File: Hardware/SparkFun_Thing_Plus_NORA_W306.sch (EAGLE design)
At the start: 81 parts, among them J1 THING_PLUS_LOGICAL, J2 LiPo, J3 QWIIC_RA, J4 SDFRICTION, J5 USB-C, J6 SWD (DNP), Q1 20V/4.2A/52mΩ/1.4W, Q2 MBT3904DW1T1, Q3 20V/4.2A/52mΩ/1.4W, Q4 20V/4.2A/52mΩ/1.4W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

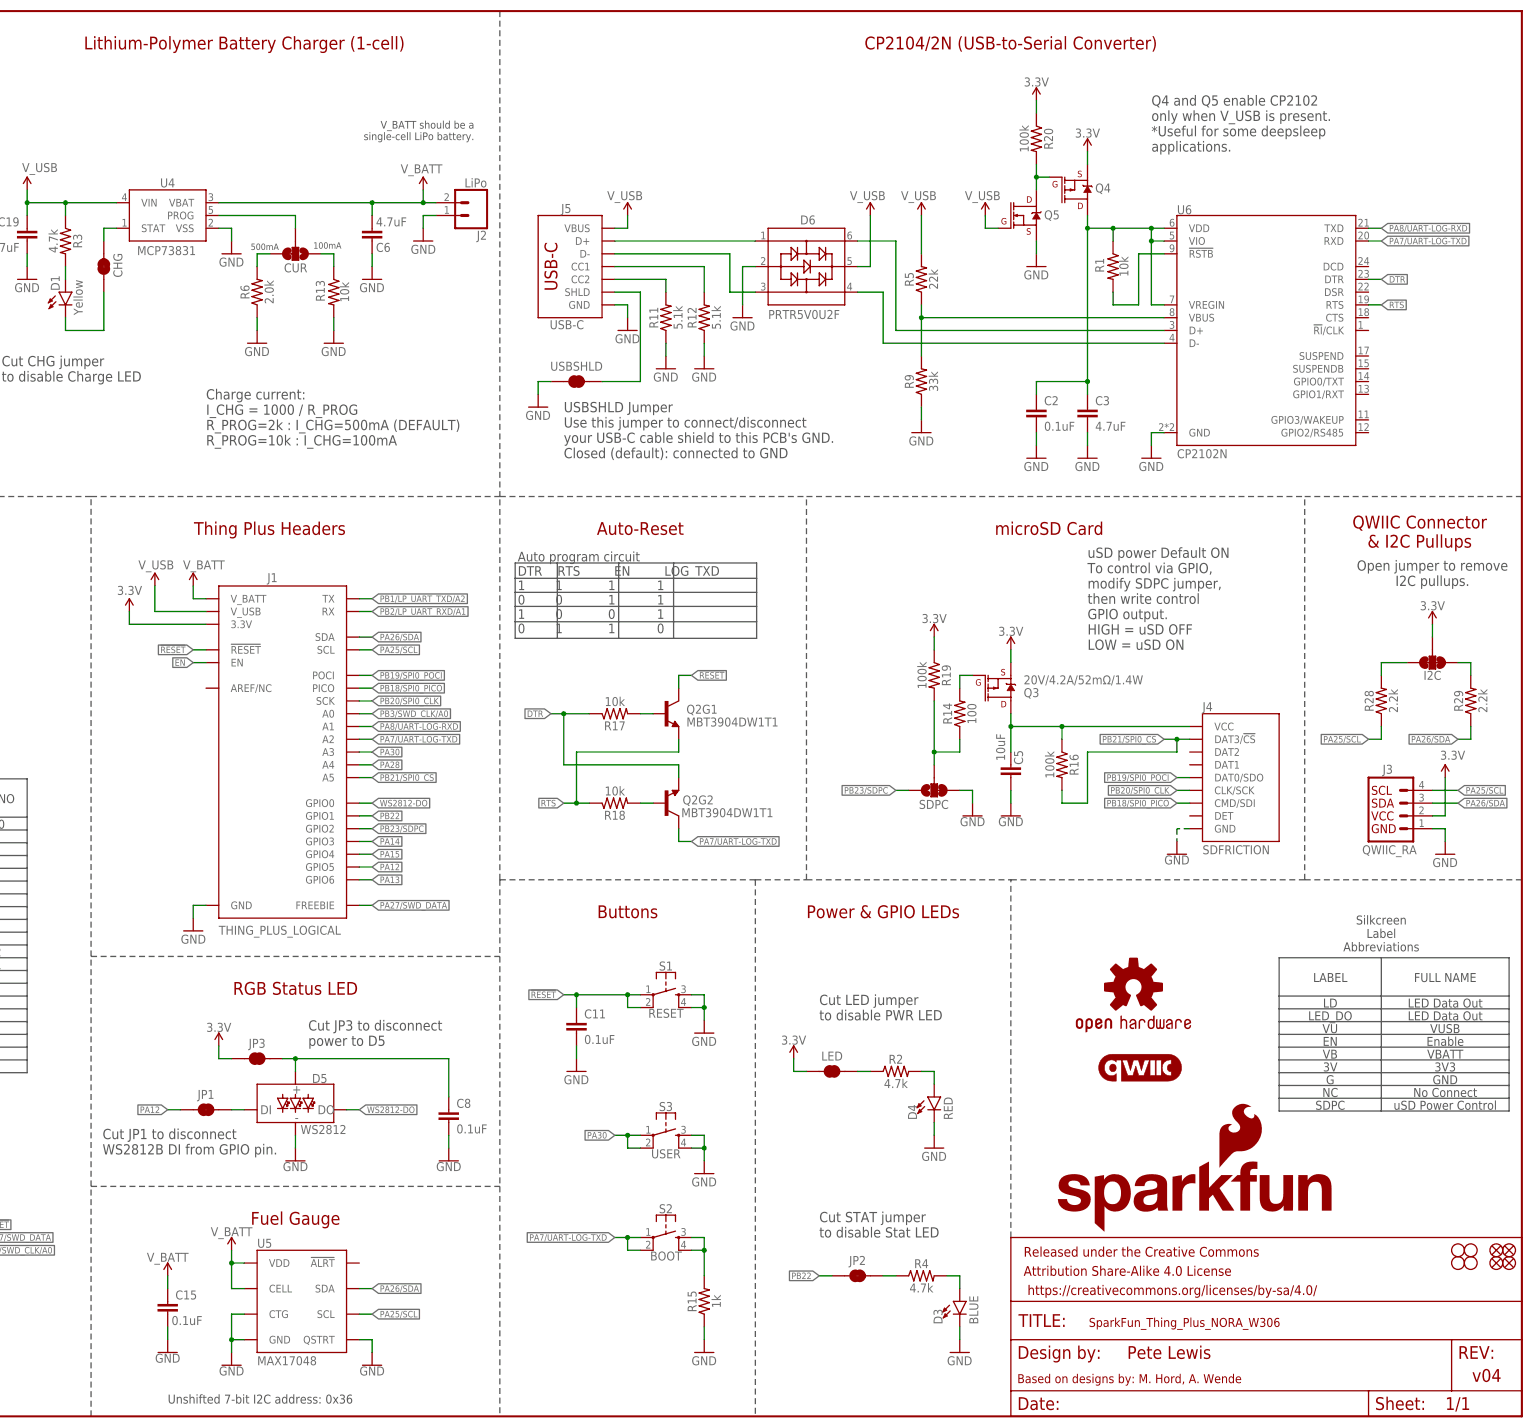
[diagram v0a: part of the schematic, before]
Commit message: final review before ordering proto changes
-added 100 ohm slow down resistor to CP2102 mosfet control gate pin
-added 1K pull down off of SCPC jumper to protect gpio in case user accidentally closes all 3 pads on jumper.
-changed VBATT trace on inner layer so it crosses SDA/SCL at 90
-added gnd via above user botton
-added full size SFE logo to bottom silk
-center product name silk
-redrew bRestrict as rectangles in module FP
-made all sch labels vector
-changed "No connect" to "Not connected" in abbreviation table
-Add note - if user cuts JP3, they should cut JP1 too to prevent back powering
-Add warning - if SDPC is enabled, user needs to not drive pins high until uSD is powered
-changed CUR jumper labels to come off the side more usually
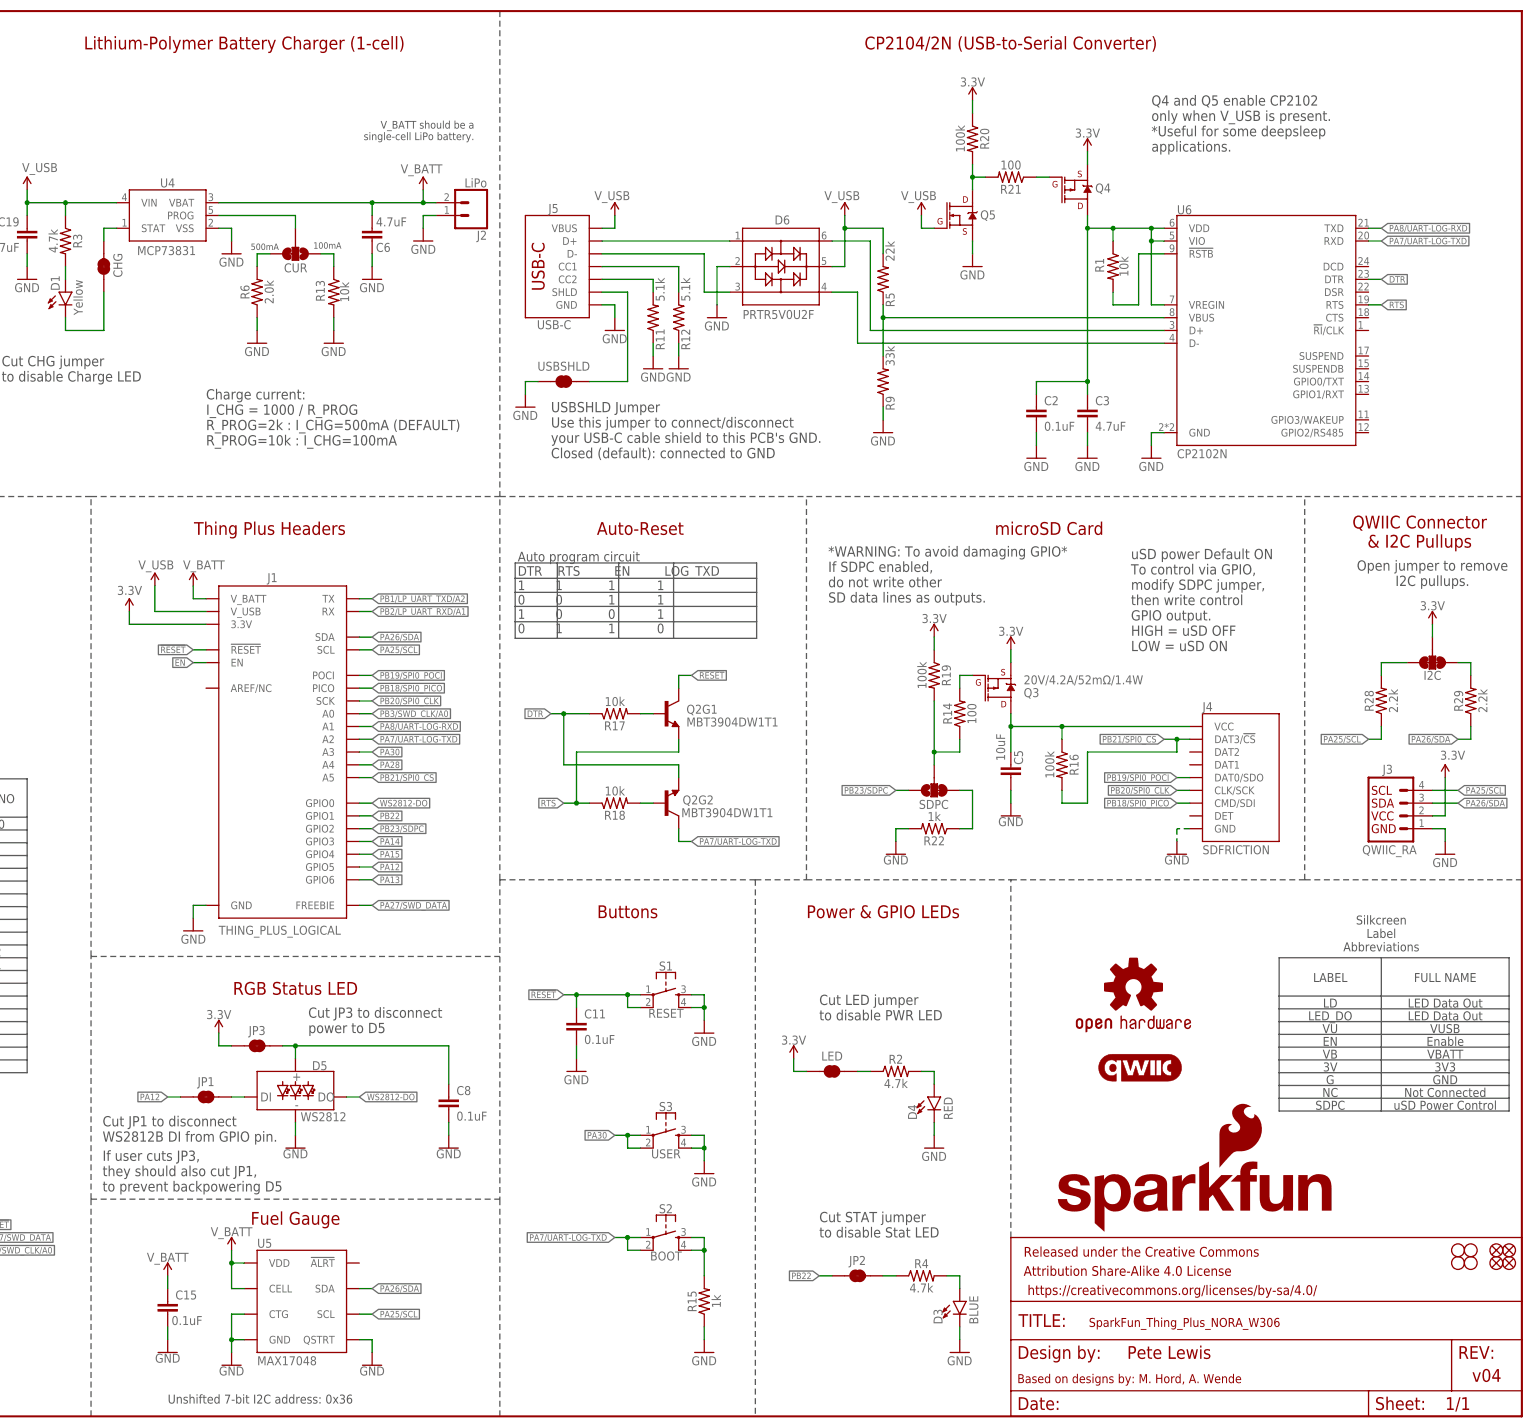
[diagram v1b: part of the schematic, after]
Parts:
- added R21: 100, SparkFun-Resistors:100OHM-0402-TIGHT-1/16W-1%
- added R22: 1k, SparkFun-Resistors:1KOHM-0402T-1/16W-1%
- LOGO3: value SFE_LOGO_NAME_FLAMEBLANK -> SFE_LOGO_NAME_FLAME.1_INCH; device SparkFun-Aesthetics:SFE_LOGO_NAME_FLAMEBLANK -> SparkFun-Aesthetics:SFE_LOGO_NAME_FLAME.1_INCH
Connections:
- new net N$30: Q4.G, R21.1
- new net N$32: R22.1, SDPC.3
- net GND: now also R22.2; no longer SDPC.3
- net N$27: now also R21.2; no longer Q4.G
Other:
- note added: "*WARNING: To avoid damaging GPIO* If SDPC enabled, do not write other SD data lines as outputs."
- note added: "If user cuts JP3, they should also cut JP1, to prevent backpowering D5"
- note added: "Not Connected"
- note removed: "No Connect"
- moved on the sheet: C8, D5, D6, J5, JP1, JP3, Q5, R11, R12, R20, R5, R9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

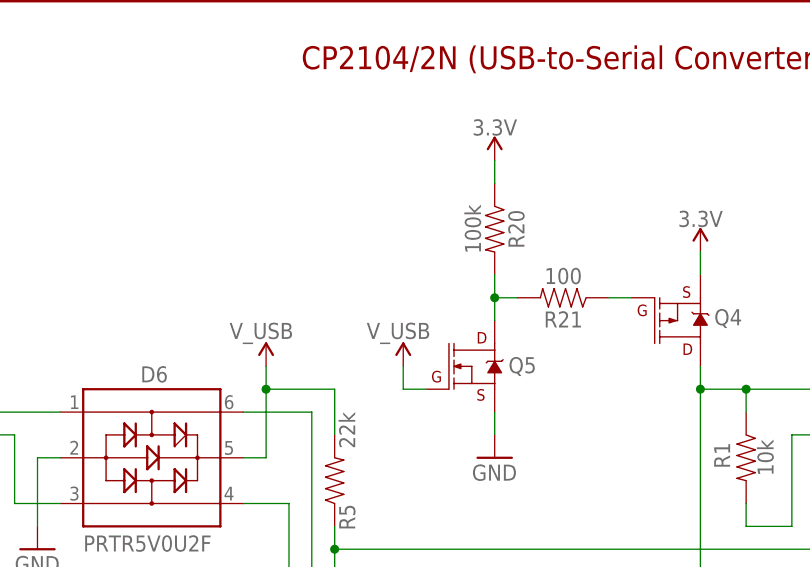
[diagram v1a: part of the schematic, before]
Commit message: added gate resistor to Q5
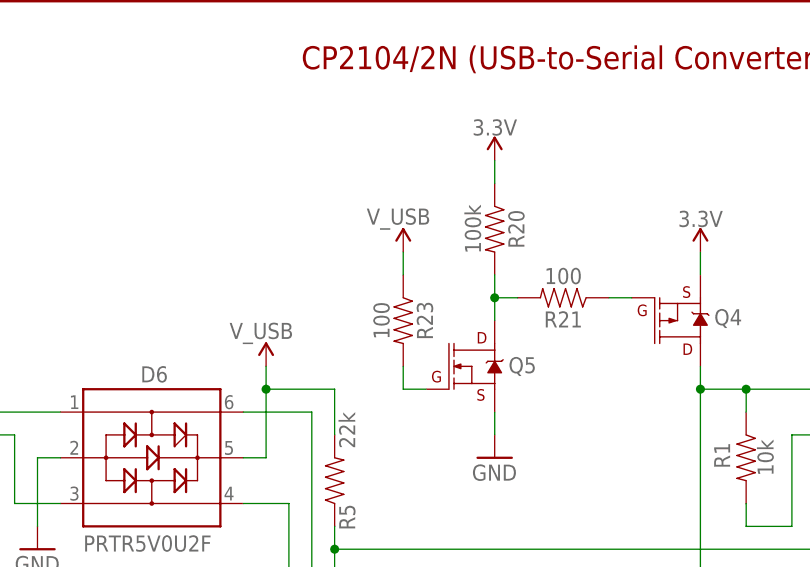
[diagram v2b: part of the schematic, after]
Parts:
- added R23: 100, SparkFun-Resistors:100OHM-0402-TIGHT-1/16W-1%
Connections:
- new net N$31: Q5.G, R23.2
- net V_USB: now also R23.1; no longer Q5.G
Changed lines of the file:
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@@
 <part name="R21" library="SparkFun-Resistors" deviceset="100OHM" device="-0402-TIGHT-1/16W-1%" value="100"/>
 <part name="R22" library="SparkFun-Resistors" deviceset="1KOHM" device="-0402T-1/16W-1%" value="1k"/>
+<part name="R23" library="SparkFun-Resistors" deviceset="100OHM" device="-0402-TIGHT-1/16W-1%" value="100"/>
 </parts>
 <sheets>
@@
 <attribute name="VALUE" x="321.056" y="254" size="1.778" layer="96" font="vector" rot="R270" align="top-center"/>
 </instance>
-<instance part="SUPPLY20" gate="G$1" x="312.42" y="238.76" smashed="yes">
-<attribute name="VALUE" x="308.356" y="241.808" size="1.778" layer="96" font="vector"/>
+<instance part="SUPPLY20" gate="G$1" x="312.42" y="251.46" smashed="yes">
+<attribute name="VALUE" x="308.356" y="254.508" size="1.778" layer="96" font="vector"/>
 </instance>
 <instance part="GND30" gate="1" x="322.58" y="228.6" smashed="yes">
@@
 <attribute name="NAME" x="314.96" y="115.316" size="1.778" layer="95" font="vector" rot="R180" align="bottom-center"/>
 <attribute name="VALUE" x="314.96" y="118.364" size="1.778" layer="96" font="vector" rot="R180" align="top-center"/>
+</instance>
+<instance part="R23" gate="G$1" x="312.42" y="243.84" smashed="yes" rot="R270">
+<attribute name="NAME" x="313.944" y="243.84" size="1.778" layer="95" font="vector" rot="R270" align="bottom-center"/>
+<attribute name="VALUE" x="310.896" y="243.84" size="1.778" layer="96" font="vector" rot="R270" align="top-center"/>
 </instance>
 </instances>
@@
 <segment>
 <pinref part="SUPPLY20" gate="G$1" pin="V_USB"/>
-<wire x1="312.42" y1="236.22" x2="312.42" y2="238.76" width="0.1524" layer="91"/>
-<pinref part="Q5" gate="NMOS" pin="G"/>
-<wire x1="314.96" y1="236.22" x2="312.42" y2="236.22" width="0.1524" layer="91"/>
+<wire x1="312.42" y1="248.92" x2="312.42" y2="251.46" width="0.1524" layer="91"/>
+<pinref part="R23" gate="G$1" pin="1"/>
 </segment>
 </net>
@@
 </segment>
 </net>
+<net name="N$31" class="0">
+<segment>
+<pinref part="Q5" gate="NMOS" pin="G"/>
+<wire x1="314.96" y1="236.22" x2="312.42" y2="236.22" width="0.1524" layer="91"/>
+<pinref part="R23" gate="G$1" pin="2"/>
+<wire x1="312.42" y1="236.22" x2="312.42" y2="238.76" width="0.1524" layer="91"/>
+</segment>
+</net>

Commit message: adjusted uSD gpio warning in SCH
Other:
- note added: "*WARNING: To avoid damaging GPIO* While uSD card is UN-powered, do not write other SPI pins as outputs."
- note removed: "*WARNING: To avoid damaging GPIO* If SDPC enabled, do not write other SD data lines as outputs."
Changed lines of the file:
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@@
 to prevent backpowering D5</text>
 <text x="293.878" y="167.386" size="2.032" layer="97" font="vector" align="center-left">*WARNING: To avoid damaging GPIO*
-If SDPC enabled,
-do not write other
-SD data lines as outputs.</text>
+While uSD card is UN-powered,
+do not write other SPI pins
+as outputs.</text>
 </plain>
 <instances>

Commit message: Via size decreased to reach 5 mil clearances
-decreased via size to provide more clearance from pads under the module
-also decrease GND traces under the module to 16 mil.
-also adjusted USB D+/D- for closer to 90 ohms impeadance (8mil trace width and 6mil gap between them).
-bumped version to v05 to keep file names straight with collaborators on this project
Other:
- note added: "v05"
- note removed: "v04"
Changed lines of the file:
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@@
 <text x="73.66" y="175.26" size="2.54" layer="94" font="vector" align="bottom-center">u-blox NORA-W306 Module</text>
 <text x="182.88" y="175.26" size="2.54" layer="94" font="vector" align="bottom-center">Thing Plus Headers</text>
-<text x="421.894" y="9.398" size="2.54" layer="94" font="vector" align="top-left">v04</text>
+<text x="421.894" y="9.398" size="2.54" layer="94" font="vector" align="top-left">v05</text>
 <text x="411.48" y="172.72" size="2.54" layer="94" font="vector" align="bottom-center">QWIIC Connector
 &amp; I2C Pullups</text>

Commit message: Bumped version to v10
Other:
- note added: "v10"
- note removed: "v05"
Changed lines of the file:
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@@
 <text x="73.66" y="175.26" size="2.54" layer="94" font="vector" align="bottom-center">u-blox NORA-W306 Module</text>
 <text x="182.88" y="175.26" size="2.54" layer="94" font="vector" align="bottom-center">Thing Plus Headers</text>
-<text x="421.894" y="9.398" size="2.54" layer="94" font="vector" align="top-left">v05</text>
+<text x="421.894" y="9.398" size="2.54" layer="94" font="vector" align="top-left">v10</text>
 <text x="411.48" y="172.72" size="2.54" layer="94" font="vector" align="bottom-center">QWIIC Connector
 &amp; I2C Pullups</text>

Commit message: Tweaks from final mini group review.
-corrected "back powering" to "powering" on sch note about JP1
-Swapped R7 from 10K to 100K for better power savings if powered from USB or 5V battery
-nudging for better GND flow
-peppered in some more gnd vias
-adjusted v_batt trace and via from header to fuel gage for better gnd flow
-adjusted SWD Traces for a little more spacing in between them
-added GND via at one layer change on SWD_DATA trace.
-switched silk to include "IO" on gpio pins (button, RGB, STAT)
-switched CUR and SDPC jumper labels to inverted text style.
-nudges bottom silk label "VB" away for better printing.
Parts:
- J3: value QWIIC_RA -> QWIIC_RIGHT_ANGLE
- R7: value 10k -> 100k; device SparkFun-Resistors:10KOHM-0402T-1/16W-1% -> SparkFun-Resistors:100KOHM-0402T-1/16W-1%
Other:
- note added: "If user cuts JP3, they should also cut JP1, to prevent powering D5"
- note removed: "If user cuts JP3, they should also cut JP1, to prevent backpowering D5"
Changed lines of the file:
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@@
 <part name="C6" library="SparkFun-Capacitors" deviceset="4.7UF" device="-0603-35V-(20%)" value="4.7uF"/>
 <part name="D2" library="SparkFun-DiscreteSemi" deviceset="DIODE-SCHOTTKY" device="-BAT20J" value="1A/23V/620mV"/>
-<part name="R7" library="SparkFun-Resistors" deviceset="10KOHM" device="-0402T-1/16W-1%" value="10k"/>
+<part name="R7" library="SparkFun-Resistors" deviceset="100KOHM" device="-0402T-1/16W-1%" value="100k"/>
 <part name="GND13" library="SparkFun-PowerSymbols" deviceset="GND" device=""/>
 <part name="J2" library="SparkFun-Connectors" deviceset="CONN_02" device="-JST-2MM-SMT" value="LiPo"/>
@@
 <part name="GND41" library="SparkFun-PowerSymbols" deviceset="GND" device=""/>
 <part name="LOGO2" library="SparkFun-Aesthetics" deviceset="OSHW-LOGO" device="M" value="OSHW-LOGOM"/>
-<part name="J3" library="SparkFun-Connectors" deviceset="QWIIC_CONNECTOR" device="JS-1MM" value="QWIIC_RA"/>
+<part name="J3" library="SparkFun-Connectors" deviceset="QWIIC_CONNECTOR" device="JS-1MM" value="QWIIC_RIGHT_ANGLE"/>
 <part name="SUPPLY1" library="SparkFun-PowerSymbols" deviceset="3.3V" device=""/>
 <part name="GND6" library="SparkFun-PowerSymbols" deviceset="GND" device=""/>
@@
 <text x="149.606" y="44.704" size="2.032" layer="97" font="vector">If user cuts JP3,
 they should also cut JP1,
-to prevent backpowering D5</text>
+to prevent powering D5</text>
 <text x="293.878" y="167.386" size="2.032" layer="97" font="vector" align="center-left">*WARNING: To avoid damaging GPIO*
 While uSD card is UN-powered,

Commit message: swapped VREG (U3) for RT9080-33
-swapped vreg (u3) for rt9080-33
-updated schematic notes to reflect new max input (5.5V)
-updated sch version to v10.1
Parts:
- U3: value XC6222B331MR-G -> RT9080-33GJ5; device SparkFun-IC-Power:XC6222B331MR-G -> SparkFun-IC-Power:V_REG_RT9080
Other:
- note added: "600mA out 5.5V max in"
- note added: "V_USB - 5.5V MAX V_BATT - Single Cell (4.2V MAX)"
- note added: "v10.1"
- note removed: "700mA out 6V max in"
- note removed: "V_USB - 6V MAX V_BATT - Single Cell (4.2V MAX)"
- note removed: "v10"
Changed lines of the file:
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@@
 <part name="D1" library="SparkFun-LED" deviceset="LED-YELLOW" device="0603" value="Yellow"/>
 <part name="R3" library="SparkFun-Resistors" deviceset="4.7KOHM" device="-0402T-1/16W-1%" value="4.7k"/>
-<part name="U3" library="SparkFun-IC-Power" deviceset="XC6222" device="B331MR-G" value="XC6222B331MR-G"/>
+<part name="U3" library="SparkFun-IC-Power" deviceset="V_REG_RT9080" device="" value="RT9080-33GJ5"/>
 <part name="Q1" library="SparkFun-DiscreteSemi" deviceset="MOSFET_PCH" device="-DMG2305UX-7" value="20V/4.2A/52mΩ/1.4W"/>
 <part name="R6" library="SparkFun-Resistors" deviceset="2.0KOHM" device="-0603-1/10W-5%" value="2.0k"/>
@@
 <text x="60.96" y="271.78" size="2.54" layer="94" font="vector" align="bottom-center">Voltage Regulator</text>
 <text x="177.8" y="271.78" size="2.54" layer="94" font="vector" align="bottom-center">Lithium-Polymer Battery Charger (1-cell)</text>
-<text x="81.28" y="205.74" size="1.778" layer="97" font="vector" align="top-center">700mA out
-6V max in</text>
+<text x="81.28" y="205.74" size="1.778" layer="97" font="vector" align="top-center">600mA out
+5.5V max in</text>
 <wire x1="0" y1="182.88" x2="121.92" y2="182.88" width="0.2032" layer="97" style="longdash"/>
 <wire x1="147.32" y1="182.88" x2="121.92" y2="182.88" width="0.2032" layer="97" style="longdash"/>
@@
 <text x="73.66" y="175.26" size="2.54" layer="94" font="vector" align="bottom-center">u-blox NORA-W306 Module</text>
 <text x="182.88" y="175.26" size="2.54" layer="94" font="vector" align="bottom-center">Thing Plus Headers</text>
-<text x="421.894" y="9.398" size="2.54" layer="94" font="vector" align="top-left">v10</text>
+<text x="421.894" y="9.398" size="2.54" layer="94" font="vector" align="top-left">v10.1</text>
 <text x="411.48" y="172.72" size="2.54" layer="94" font="vector" align="bottom-center">QWIIC Connector
 &amp; I2C Pullups</text>
@@
 <text x="304.8" y="99.06" size="2.54" layer="94" font="vector" align="bottom-center">Power &amp; GPIO LEDs</text>
 <text x="331.47" y="6.604" size="1.778" layer="94" font="vector">Based on designs by: M. Hord, A. Wende</text>
-<text x="60.96" y="264.16" size="1.778" layer="97" font="vector" align="bottom-center">V_USB - 6V MAX
+<text x="60.96" y="264.16" size="1.778" layer="97" font="vector" align="bottom-center">V_USB - 5.5V MAX
 V_BATT - Single Cell (4.2V MAX)</text>
 <text x="191.516" y="232.156" size="1.27" layer="97" font="vector">100mA</text>
